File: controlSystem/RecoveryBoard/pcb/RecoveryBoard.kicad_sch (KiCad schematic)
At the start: 1 part

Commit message: v3.1. Cap to deal with spikes on RBF, 100k on main Q pull down, better notes on schematic for part numbers, moved Vbatt pickoff to after main Q.
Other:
- title: (none) -> Electromechanical Recovery System Board

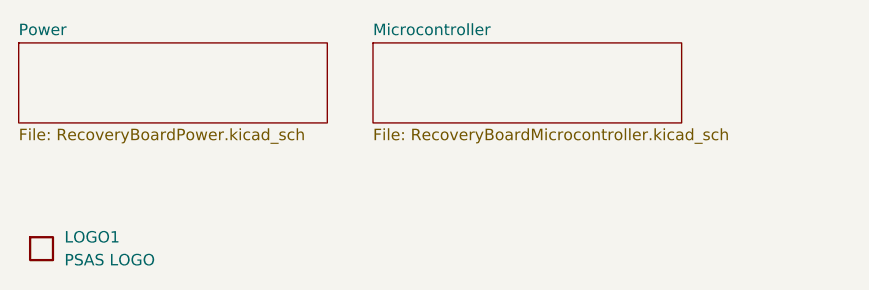
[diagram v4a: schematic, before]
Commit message: Stuffing four more v3.0 PCBs and discovered everything wasn't updated. Fixed BOM, fixed a lot of schematic errors especially in symbols, fixed some footprint errors, synchronized schematic and pcb, and general cleanup. This board is still v3.1.
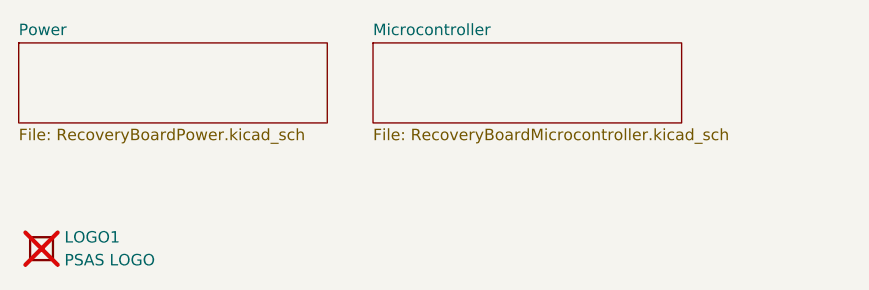
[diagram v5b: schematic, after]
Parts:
- LOGO1: now not fitted
